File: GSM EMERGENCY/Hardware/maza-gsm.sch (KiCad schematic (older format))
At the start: 257 parts, among them J1 SIM_Card, J10 ON_OFF_SWITCH, J11 LED2, J12 LED3, J13 LED4, J14 LED5, J15 LED6, J16 LED7, J17 LED8, J18 OLED CONNECTOR, J19 PB1, J2 NETWORK_LED, J20 PB2, J21 PB3, J22 PB4, J23 OLED_INDICATOR, J24 32Ohm,Speaker, J25 8OHM, SPEAKER, J26 2.2Kohms, Load Res.Mic, J27 ICSP, J3 PCM CON, J4 SD CON, J5 1PPS_LED, J6 SIM_Card, J7 USB_OTG, J8 POWER_ADAPTER, J9 LED1, Q1 BC847, Q10 BC847, Q11 BC847, Q12 BC847, Q13 BC847, Q2 BC847, Q3 BC857, Q4 BC847, Q5 BC847, Q6 BC847, Q7 BC847, Q8 BC847, Q9 BC847, U1 MIC29302_LDO, U2 MC60, U3 SGM2019_LDO, U4 Audio_Jack3.5mm, U5 MAX8903A, U6 LM3940, U7 PIC32MX440F512H, U8 MAX734, X1 oscillator_DSC1033

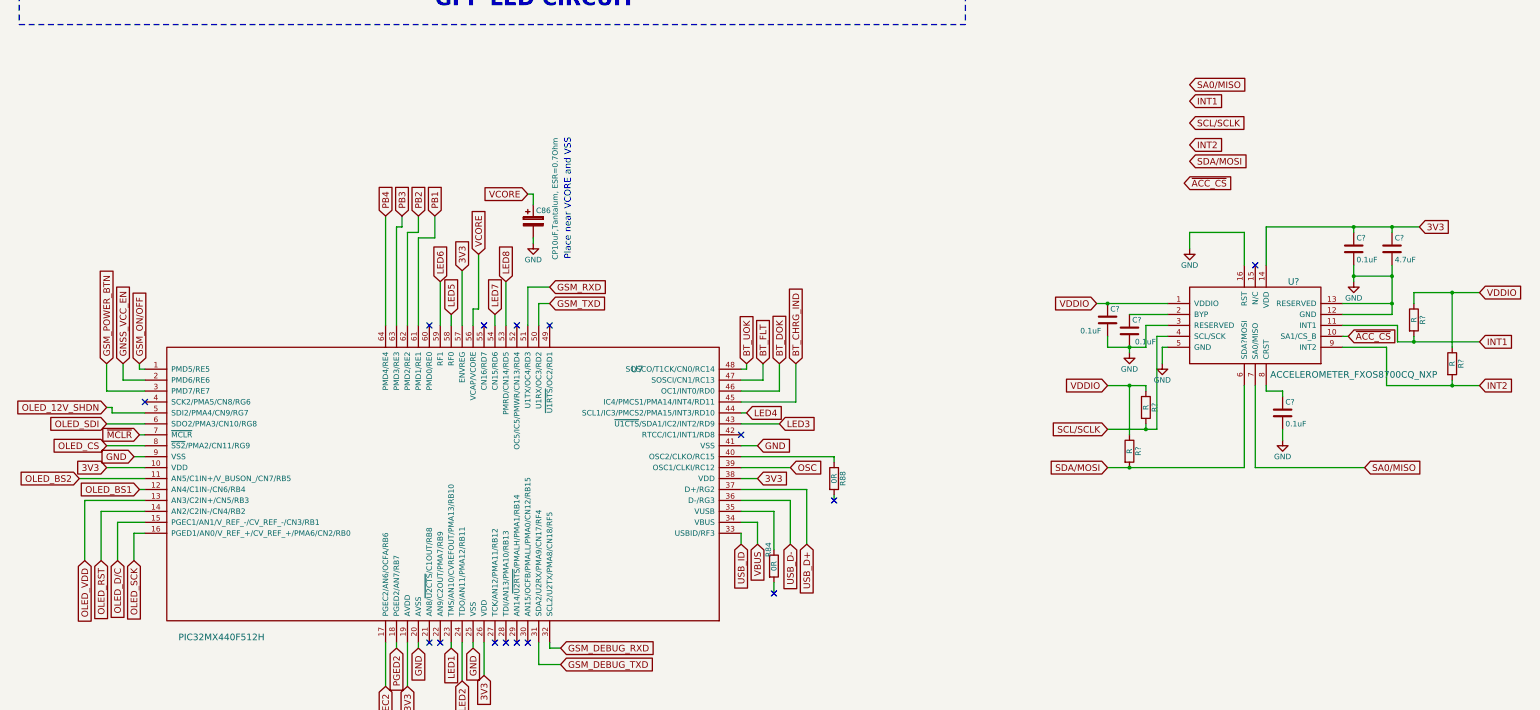
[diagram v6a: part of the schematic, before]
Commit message: Loaded netlist to pcbnew and sorted components, added pcb keepout
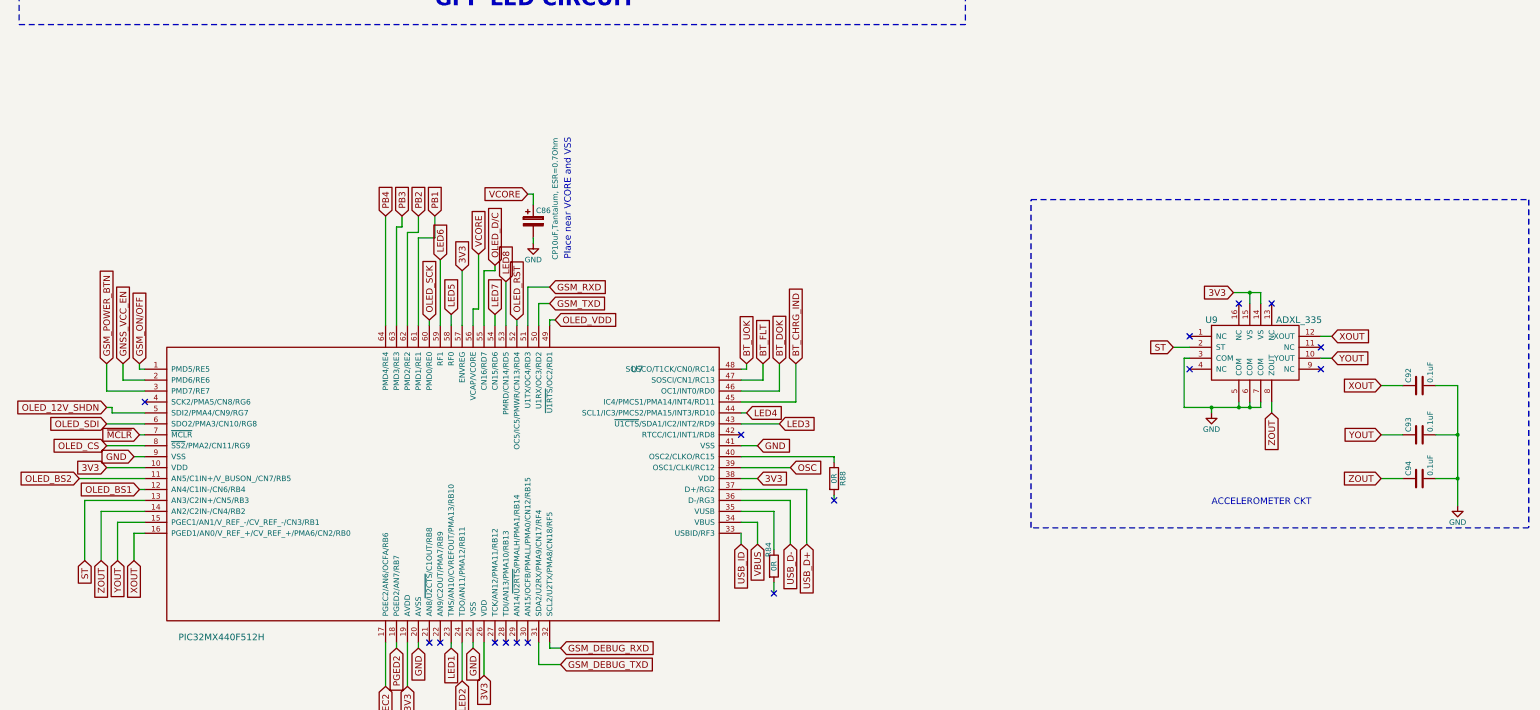
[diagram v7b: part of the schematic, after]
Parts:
- removed C? (x4): 0.1uF, symbol C
- removed C?: 4.7uF, symbol C
- removed R? (x4): R, symbol R
- removed U?: ACCELEROMETER_FXOS8700CQ_NXP, symbol ACCELEROMETER_FXOS8700CQ_NXP
- added C92, C93, C94: 0.1uF, Capacitors_SMD:C_0805_HandSoldering, symbol C
- added U9: ADXL_335, Housings_DFN_QFN:QFN-16-1EP_4x4mm_Pitch0.65mm, symbol ADXL_335
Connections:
- net 3V3: now also U9.14 (VS), U9.15 (VS)
- net GND: now also C92.2, C93.2, C94.2, U9.3 (COM), U9.5 (COM), U9.6 (COM), U9.7 (COM)
- net OLED_D/C: now also U7.55 (CN16/RD7); no longer U7.15 (PGEC1/AN1/V_REF_-/CV_REF_-/CN3/RB1)
- net OLED_RST: now also U7.52 (OC5/IC5/PMWR/CN13/RD4); no longer U7.14 (AN2/C2IN-/CN4/RB2)
- net OLED_SCK: now also U7.60 (PMD0/RE0); no longer U7.16 (PGED1/AN0/V_REF_+/CV_REF_+/PMA6/CN2/RB0)
- net OLED_VDD: now also U7.49 (~U1RTS~/OC2/RD1); no longer U7.13 (AN3/C2IN+/CN5/RB3)
- new net ST: U7.13 (AN3/C2IN+/CN5/RB3), U9.2 (ST)
- new net XOUT: C92.1, U7.16 (PGED1/AN0/V_REF_+/CV_REF_+/PMA6/CN2/RB0), U9.12 (XOUT)
- new net YOUT: C93.1, U7.15 (PGEC1/AN1/V_REF_-/CV_REF_-/CN3/RB1), U9.10 (YOUT)
- new net ZOUT: C94.1, U7.14 (AN2/C2IN-/CN4/RB2), U9.8 (ZOUT)
- no-connect marks 44 -> 45
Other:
- note added: "ACCELEROMETER CKT"

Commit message: PCB completed
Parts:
- added P1, P2, P3, P4: TH_PAD, kicad_libraries:TH_HOLE_PAD_5.5mm, symbol TH_PAD
- added P5, P6, P7, P8: TH_PAD, kicad_libraries:TH_HOLE_PAD_6.5mm, symbol TH_PAD
- BT1: footprint Pin_Headers:Pin_Header_Straight_1x02_Pitch2.54mm -> kicad_libraries:BATTERTY_PAD_SMD
- J10: footprint Connectors_Terminal_Blocks:TerminalBlock_Pheonix_MPT-2.54mm_3pol -> kicad_libraries:SMD_2PIN_SWITCH
- J11, J12, J13, J14, J15, J16, J17, J9: footprint Connectors_Terminal_Blocks:TerminalBlock_Pheonix_MPT-2.54mm_2pol -> Resistors_SMD:R_0805_HandSoldering
- J19, J20, J21, J22: footprint Pin_Headers:Pin_Header_Straight_1x02_Pitch2.54mm -> Resistors_SMD:R_0805_HandSoldering
- J8: footprint Connectors_Terminal_Blocks:TerminalBlock_Pheonix_MPT-2.54mm_2pol -> kicad_libraries:BATTERTY_PAD_SMD
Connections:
- wire segments 912 -> 914
- no-connect marks 45 -> 53
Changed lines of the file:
@@
 F 0 "BT1" H 18650 21450 50  0000 L CNN
 F 1 "Battery_Cell" H 18650 21350 50  0000 L CNN
-F 2 "Pin_Headers:Pin_Header_Straight_1x02_Pitch2.54mm" V 18550 21410 50  0001 C CNN
+F 2 "kicad_libraries:BATTERTY_PAD_SMD" V 18550 21410 50  0001 C CNN
 F 3 "" V 18550 21410 50  0001 C CNN
 	1    18550 21350
@@
 F 0 "J8" H 15550 18650 50  0000 C CNN
 F 1 "POWER_ADAPTER" V 15650 18500 50  0000 C CNN
-F 2 "Connectors_Terminal_Blocks:TerminalBlock_Pheonix_MPT-2.54mm_2pol" H 15550 18500 50  0001 C CNN
+F 2 "kicad_libraries:BATTERTY_PAD_SMD" H 15550 18500 50  0001 C CNN
 F 3 "" H 15550 18500 50  0001 C CNN
 	1    15550 18500
 	-1   0    0    1
 $EndComp
-Text GLabel 15850 18450 2    60   Input ~ 0
+Text GLabel 15800 18550 2    60   Input ~ 0
 USB_ADAPTER
 $Comp
 L GND #PWR055
 U 1 1 58F45202
-P 15850 18600
-F 0 "#PWR055" H 15850 18350 50  0001 C CNN
-F 1 "GND" H 15850 18450 50  0000 C CNN
-F 2 "" H 15850 18600 50  0001 C CNN
-F 3 "" H 15850 18600 50  0001 C CNN
-	1    15850 18600
+P 15950 18300
+F 0 "#PWR055" H 15950 18050 50  0001 C CNN
+F 1 "GND" H 15950 18150 50  0000 C CNN
+F 2 "" H 15950 18300 50  0001 C CNN
+F 3 "" H 15950 18300 50  0001 C CNN
+	1    15950 18300
 	1    0    0    -1
 $EndComp
@@
 F 0 "J9" H 18550 6400 50  0000 C CNN
 F 1 "LED1" V 18650 6350 50  0000 C CNN
-F 2 "Connectors_Terminal_Blocks:TerminalBlock_Pheonix_MPT-2.54mm_2pol" H 18550 6250 50  0001 C CNN
+F 2 "Resistors_SMD:R_0805_HandSoldering" H 18550 6250 50  0001 C CNN
 F 3 "" H 18550 6250 50  0001 C CNN
 	1    18550 6250
@@
 F 0 "J11" H 19450 6400 50  0000 C CNN
 F 1 "LED2" V 19550 6350 50  0000 C CNN
-F 2 "Connectors_Terminal_Blocks:TerminalBlock_Pheonix_MPT-2.54mm_2pol" H 19450 6250 50  0001 C CNN
+F 2 "Resistors_SMD:R_0805_HandSoldering" H 19450 6250 50  0001 C CNN
 F 3 "" H 19450 6250 50  0001 C CNN
 	1    19450 6250
@@
 F 0 "J12" H 20400 6400 50  0000 C CNN
 F 1 "LED3" V 20500 6350 50  0000 C CNN
-F 2 "Connectors_Terminal_Blocks:TerminalBlock_Pheonix_MPT-2.54mm_2pol" H 20400 6250 50  0001 C CNN
+F 2 "Resistors_SMD:R_0805_HandSoldering" H 20400 6250 50  0001 C CNN
 F 3 "" H 20400 6250 50  0001 C CNN
 	1    20400 6250
@@
 F 0 "J13" H 21350 6400 50  0000 C CNN
 F 1 "LED4" V 21450 6350 50  0000 C CNN
-F 2 "Connectors_Terminal_Blocks:TerminalBlock_Pheonix_MPT-2.54mm_2pol" H 21350 6250 50  0001 C CNN
+F 2 "Resistors_SMD:R_0805_HandSoldering" H 21350 6250 50  0001 C CNN
 F 3 "" H 21350 6250 50  0001 C CNN
 	1    21350 6250
@@
 F 0 "J14" H 22400 6450 50  0000 C CNN
 F 1 "LED5" V 22500 6400 50  0000 C CNN
-F 2 "Connectors_Terminal_Blocks:TerminalBlock_Pheonix_MPT-2.54mm_2pol" H 22400 6300 50  0001 C CNN
+F 2 "Resistors_SMD:R_0805_HandSoldering" H 22400 6300 50  0001 C CNN
 F 3 "" H 22400 6300 50  0001 C CNN
 	1    22400 6300
@@
 F 0 "J15" H 23300 6450 50  0000 C CNN
 F 1 "LED6" V 23400 6400 50  0000 C CNN
-F 2 "Connectors_Terminal_Blocks:TerminalBlock_Pheonix_MPT-2.54mm_2pol" H 23300 6300 50  0001 C CNN
+F 2 "Resistors_SMD:R_0805_HandSoldering" H 23300 6300 50  0001 C CNN
 F 3 "" H 23300 6300 50  0001 C CNN
 	1    23300 6300
@@
 F 0 "J16" H 24250 6450 50  0000 C CNN
 F 1 "LED7" V 24350 6400 50  0000 C CNN
-F 2 "Connectors_Terminal_Blocks:TerminalBlock_Pheonix_MPT-2.54mm_2pol" H 24250 6300 50  0001 C CNN
+F 2 "Resistors_SMD:R_0805_HandSoldering" H 24250 6300 50  0001 C CNN
 F 3 "" H 24250 6300 50  0001 C CNN
 	1    24250 6300
@@
 F 0 "J17" H 25200 6450 50  0000 C CNN
 F 1 "LED8" V 25300 6400 50  0000 C CNN
-F 2 "Connectors_Terminal_Blocks:TerminalBlock_Pheonix_MPT-2.54mm_2pol" H 25200 6300 50  0001 C CNN
+F 2 "Resistors_SMD:R_0805_HandSoldering" H 25200 6300 50  0001 C CNN
 F 3 "" H 25200 6300 50  0001 C CNN
 	1    25200 6300
@@
 F 0 "J10" H 18900 20950 50  0000 C CNN
 F 1 "ON_OFF_SWITCH" V 19000 20750 50  0000 C CNN
-F 2 "Connectors_Terminal_Blocks:TerminalBlock_Pheonix_MPT-2.54mm_3pol" H 18900 20750 50  0001 C CNN
+F 2 "kicad_libraries:SMD_2PIN_SWITCH" H 18900 20750 50  0001 C CNN
 F 3 "" H 18900 20750 50  0001 C CNN
 	1    18900 20750
@@
 F 0 "J22" H 16900 7050 50  0000 C CNN
 F 1 "PB4" V 17000 6900 50  0000 C CNN
-F 2 "Pin_Headers:Pin_Header_Straight_1x02_Pitch2.54mm" H 16900 6900 50  0001 C CNN
+F 2 "Resistors_SMD:R_0805_HandSoldering" H 16900 6900 50  0001 C CNN
 F 3 "" H 16900 6900 50  0001 C CNN
 	1    16900 6900
@@
 F 0 "J21" H 16200 7050 50  0000 C CNN
 F 1 "PB3" V 16300 6900 50  0000 C CNN
-F 2 "Pin_Headers:Pin_Header_Straight_1x02_Pitch2.54mm" H 16200 6900 50  0001 C CNN
+F 2 "Resistors_SMD:R_0805_HandSoldering" H 16200 6900 50  0001 C CNN
 F 3 "" H 16200 6900 50  0001 C CNN
 	1    16200 6900
@@
 F 0 "J20" H 15500 7050 50  0000 C CNN
 F 1 "PB2" V 15600 6900 50  0000 C CNN
-F 2 "Pin_Headers:Pin_Header_Straight_1x02_Pitch2.54mm" H 15500 6900 50  0001 C CNN
+F 2 "Resistors_SMD:R_0805_HandSoldering" H 15500 6900 50  0001 C CNN
 F 3 "" H 15500 6900 50  0001 C CNN
 	1    15500 6900
@@
 F 0 "J19" H 14800 7050 50  0000 C CNN
 F 1 "PB1" V 14900 6900 50  0000 C CNN
-F 2 "Pin_Headers:Pin_Header_Straight_1x02_Pitch2.54mm" H 14800 6900 50  0001 C CNN
+F 2 "Resistors_SMD:R_0805_HandSoldering" H 14800 6900 50  0001 C CNN
 F 3 "" H 14800 6900 50  0001 C CNN
 	1    14800 6900
@@
 Wire Wire Line
 	14500 20700 14500 20800
-Wire Wire Line
-	15750 18450 15850 18450
-Wire Wire Line
-	15850 18550 15850 18600
-Wire Wire Line
-	15750 18550 15850 18550
 Connection ~ 16650 20750
 Wire Wire Line
@@
 Wire Wire Line
 	22700 11200 22700 11250
+Wire Wire Line
+	15750 18450 15800 18450
+Wire Wire Line
+	15800 18450 15800 18200
+Wire Wire Line
+	15800 18200 15950 18200
+Wire Wire Line
+	15950 18200 15950 18300
+Wire Wire Line
+	15800 18550 15750 18550
+$Comp
+L TH_PAD P1
+U 1 1 59102BBF
+P 32050 17450
+F 0 "P1" H 32100 17550 60  0000 C CNN
+F 1 "TH_PAD" H 32050 17350 60  0000 C CNN
+F 2 "kicad_libraries:TH_HOLE_PAD_5.5mm" H 32000 17450 60  0001 C CNN
+F 3 "" H 32000 17450 60  0001 C CNN
+	1    32050 17450
+	1    0    0    -1
+$EndComp
+$Comp
+L TH_PAD P2
+U 1 1 591032CC
+P 32050 17750
+F 0 "P2" H 32100 17850 60  0000 C CNN
+F 1 "TH_PAD" H 32050 17650 60  0000 C CNN
+F 2 "kicad_libraries:TH_HOLE_PAD_5.5mm" H 32000 17750 60  0001 C CNN
+F 3 "" H 32000 17750 60  0001 C CNN
+	1    32050 17750
+	1    0    0    -1
+$EndComp
+$Comp
+L TH_PAD P3
+U 1 1 591034ED
+P 32050 18050
+F 0 "P3" H 32100 18150 60  0000 C CNN
+F 1 "TH_PAD" H 32050 17950 60  0000 C CNN
+F 2 "kicad_libraries:TH_HOLE_PAD_5.5mm" H 32000 18050 60  0001 C CNN
+F 3 "" H 32000 18050 60  0001 C CNN
+	1    32050 18050
+	1    0    0    -1
+$EndComp
+$Comp
+L TH_PAD P4
+U 1 1 5910370C
+P 32050 18350
+F 0 "P4" H 32100 18450 60  0000 C CNN
+F 1 "TH_PAD" H 32050 18250 60  0000 C CNN
+F 2 "kicad_libraries:TH_HOLE_PAD_5.5mm" H 32000 18350 60  0001 C CNN
+F 3 "" H 32000 18350 60  0001 C CNN
+	1    32050 18350
+	1    0    0    -1
+$EndComp
+$Comp
+L TH_PAD P5
+U 1 1 5910392D
+P 32050 19200
+F 0 "P5" H 32100 19300 60  0000 C CNN
+F 1 "TH_PAD" H 32050 19100 60  0000 C CNN
+F 2 "kicad_libraries:TH_HOLE_PAD_6.5mm" H 32000 19200 60  0001 C CNN
+F 3 "" H 32000 19200 60  0001 C CNN
+	1    32050 19200
+	1    0    0    -1
+$EndComp
+$Comp
+L TH_PAD P6
+U 1 1 59103B4E
+P 32050 19500
+F 0 "P6" H 32100 19600 60  0000 C CNN
+F 1 "TH_PAD" H 32050 19400 60  0000 C CNN
+F 2 "kicad_libraries:TH_HOLE_PAD_6.5mm" H 32000 19500 60  0001 C CNN
+F 3 "" H 32000 19500 60  0001 C CNN
+	1    32050 19500
+	1    0    0    -1
+$EndComp
+$Comp
+L TH_PAD P7
+U 1 1 59103D6D
+P 32050 19800
+F 0 "P7" H 32100 19900 60  0000 C CNN
+F 1 "TH_PAD" H 32050 19700 60  0000 C CNN
+F 2 "kicad_libraries:TH_HOLE_PAD_6.5mm" H 32000 19800 60  0001 C CNN
+F 3 "" H 32000 19800 60  0001 C CNN
+	1    32050 19800
+	1    0    0    -1
+$EndComp
+$Comp
+L TH_PAD P8
+U 1 1 59103F96
+P 32050 20100
+F 0 "P8" H 32100 20200 60  0000 C CNN
+F 1 "TH_PAD" H 32050 20000 60  0000 C CNN
+F 2 "kicad_libraries:TH_HOLE_PAD_6.5mm" H 32000 20100 60  0001 C CNN
+F 3 "" H 32000 20100 60  0001 C CNN
+	1    32050 20100
+	1    0    0    -1
+$EndComp
+NoConn ~ 31750 17450
+NoConn ~ 31750 17750
+NoConn ~ 31750 18050
+NoConn ~ 31750 18350
+NoConn ~ 31750 19200
+NoConn ~ 31750 19500
+NoConn ~ 31750 19800
+NoConn ~ 31750 20100
 $EndSCHEMATC
